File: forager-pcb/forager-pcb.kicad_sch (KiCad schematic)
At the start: 76 parts, among them J1 Conn_01x02_Pin, J2 Conn_01x02_Pin

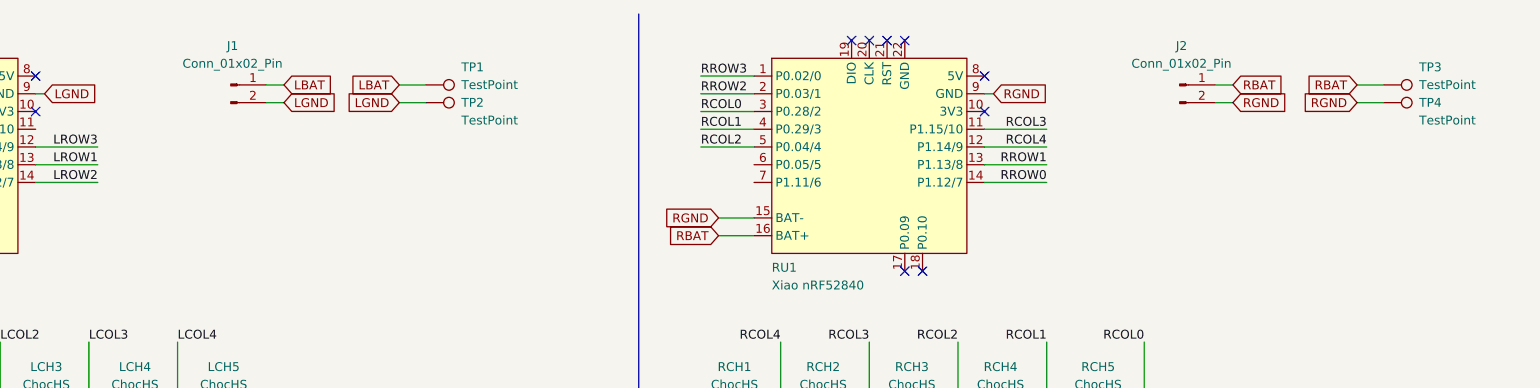
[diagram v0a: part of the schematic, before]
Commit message: add a power switch, change the battery test points to through hole
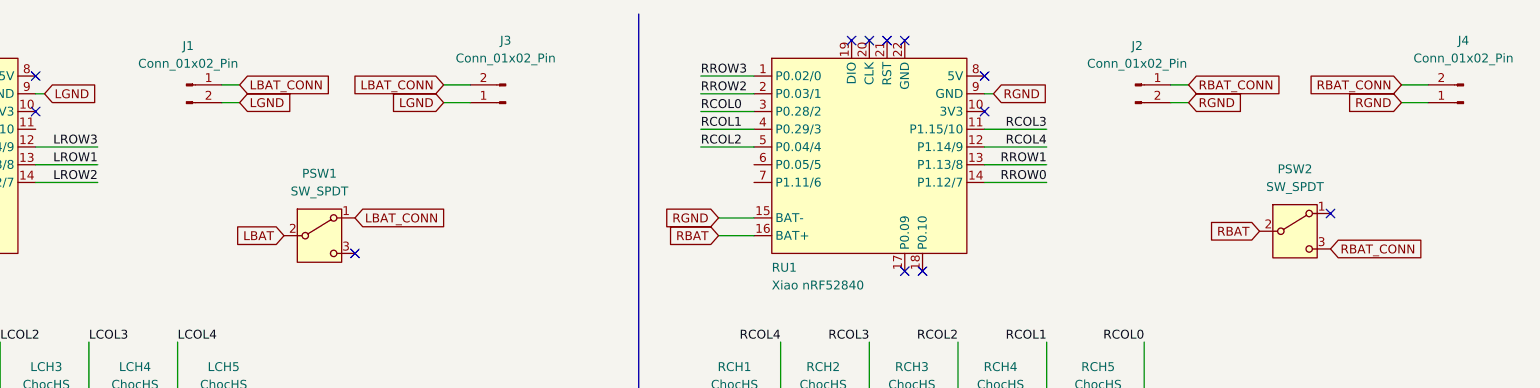
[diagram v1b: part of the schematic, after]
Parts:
- removed TP1, TP2, TP3, TP4: TestPoint, TestPoint:TestPoint_Pad_D2.0mm, symbol Connector:TestPoint
- added J3, J4: Conn_01x02_Pin, Connector_PinHeader_2.54mm:PinHeader_1x02_P2.54mm_Vertical, symbol Connector:Conn_01x02_Pin
- added PSW1, PSW2: SW_SPDT, PCM_marbastlib-various:SW_MSK12C02-HB, symbol Switch:SW_SPDT
- J1, J2: LCSC (none) -> C5118738
- LCH1, LCH10, LCH11, LCH12, LCH13, LCH14, LCH15, LCH16, LCH17, LCH2, LCH3, LCH4, LCH5, LCH6, LCH7, LCH8, LCH9, RCH1, RCH10, RCH11, RCH12, RCH13, RCH14, RCH15, RCH16, RCH17, RCH2, RCH3, RCH4, RCH5, RCH6, RCH7, RCH8, RCH9: LCSC (none) -> C5333465
- LD1, LD10, LD11, LD12, LD13, LD14, LD15, LD16, LD17, LD2, LD3, LD4, LD5, LD6, LD7, LD8, LD9, RD1, RD10, RD11, RD12, RD13, RD14, RD15, RD16, RD17, RD2, RD3, RD4, RD5, RD6, RD7, RD8, RD9: LCSC (none) -> C81598
- LU1, RU1: LCSC (none) -> N/A
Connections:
- net LBAT: now also PSW1.2 (B); no longer J1.1 (Pin_1)
- net LGND: now also J3.1 (Pin_1)
- net RBAT: now also PSW2.2 (B); no longer J2.1 (Pin_1)
- net RGND: now also J4.1 (Pin_1)
- new net LBAT_CONN: J1.1 (Pin_1), J3.2 (Pin_2), PSW1.1 (A)
- new net RBAT_CONN: J2.1 (Pin_1), J4.2 (Pin_2), PSW2.3 (C)
- no-connect marks 16 -> 18
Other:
- moved on the sheet: J1, J2
